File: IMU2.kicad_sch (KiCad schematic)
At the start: 3 parts, among them U3 262-BMI088

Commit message: multiple chainges on PCB
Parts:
- added BMI3, BMI3_SCL1, BMI3_SDA1: 0, Resistor_SMD:R_0603_1608Metric, symbol #dzdb:g_res/R-0-0603
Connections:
- net BMI_IN_3.3V: now also BMI3.1; no longer U3.14 (CSB1), U3.7 (PS)
- net IMU_SCL: now also BMI3_SCL1.1; no longer U3.8 (SCL/SCK)
- net IMU_SDA: now also BMI3_SDA1.1; no longer U3.9 (SDA/SDI)
- new net: BMI3_SCL1.2, U3.8 (SCL/SCK)
- new net: BMI3.2, U3.14 (CSB1), U3.7 (PS)
- new net: BMI3_SDA1.2, U3.9 (SDA/SDI)

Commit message: nearly complete with the PCB
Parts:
- renumbered BMI3 to BMI2, BMI3_SCL1 to BMI2_SCL1, BMI3_SDA1 to BMI2_SDA1, U3 to U2
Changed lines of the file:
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@@
 		(on_board yes)
 		(dnp no)
-		(property "Reference" "BMI3_SCL1"
+		(property "Reference" "BMI2_SCL1"
 			(at 119.38 99.06 90)
 			(effects
@@
 			(project "nautilus_mainboard"
 				(path "/ce1819b2-f280-40ed-834f-6fe4d12f809d/bdf8f7d6-a5ee-4741-925d-5019e8cbdfce/a7ffb13a-d9ae-4b81-b70f-0aefcfc6ef00"
-					(reference "BMI3_SCL1")
+					(reference "BMI2_SCL1")
 					(unit 1)
 				)
@@
 		(on_board yes)
 		(dnp no)
-		(property "Reference" "BMI3"
+		(property "Reference" "BMI2"
 			(at 119.38 88.9 90)
 			(effects
@@
 			(project "nautilus_mainboard"
 				(path "/ce1819b2-f280-40ed-834f-6fe4d12f809d/bdf8f7d6-a5ee-4741-925d-5019e8cbdfce/a7ffb13a-d9ae-4b81-b70f-0aefcfc6ef00"
-					(reference "BMI3")
+					(reference "BMI2")
 					(unit 1)
 				)
@@
 		(on_board yes)
 		(dnp no)
-		(property "Reference" "BMI3_SDA1"
+		(property "Reference" "BMI2_SDA1"
 			(at 119.38 101.6 90)
 			(effects
@@
 			(project "nautilus_mainboard"
 				(path "/ce1819b2-f280-40ed-834f-6fe4d12f809d/bdf8f7d6-a5ee-4741-925d-5019e8cbdfce/a7ffb13a-d9ae-4b81-b70f-0aefcfc6ef00"
-					(reference "BMI3_SDA1")
+					(reference "BMI2_SDA1")
 					(unit 1)
 				)
@@
 		(dnp no)
 		(fields_autoplaced yes)
-		(property "Reference" "U3"
+		(property "Reference" "U2"
 			(at 144.78 73.66 0)
 			(effects
@@
 			(project "nautilus_mainboard"
 				(path "/ce1819b2-f280-40ed-834f-6fe4d12f809d/bdf8f7d6-a5ee-4741-925d-5019e8cbdfce/a7ffb13a-d9ae-4b81-b70f-0aefcfc6ef00"
-					(reference "U3")
+					(reference "U2")
 					(unit 1)
 				)

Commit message: chore: Many routing changes
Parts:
- removed BMI2, BMI2_SCL1, BMI2_SDA1: 0, Resistor_SMD:R_0603_1608Metric, symbol #dzdb:g_res/R-0-0603
- added R48, R49, R52: 0, Resistor_SMD:R_0603_1608Metric, symbol #dzdb:g_res/R-0-0603
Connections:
- net IMU_SCL: now also R48.1
- net IMU_SDA: now also R49.1
- net at U2.8 (SCL/SCK): now also R48.2
- net at U2.14 (CSB1), U2.7 (PS): now also R52.2
- net at U2.9 (SDA/SDI): now also R49.2
- net BMI_IN_3.3V renamed BMI_In_3.3V
- net BMI_In_3.3V: now also R52.1

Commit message: chore: more cleanup
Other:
- company: (none) -> Davide
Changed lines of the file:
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@@
 	(generator_version "9.0")
 	(paper "A4")
+	(title_block
+		(date "2025-11-18")
+		(company "Davide")
+	)
 	(text "Acc: 0x19\nGyro: 0x69"
 		(exclude_from_sim no)

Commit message: chore: Loads of redoing stuff. Added a Changelog
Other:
- title: (none) -> Nautilus_Mainboard
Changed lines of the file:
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@@
 	(paper "A4")
 	(title_block
+		(title "Nautilus_Mainboard")
 		(date "2025-11-19")
 		(rev "0")

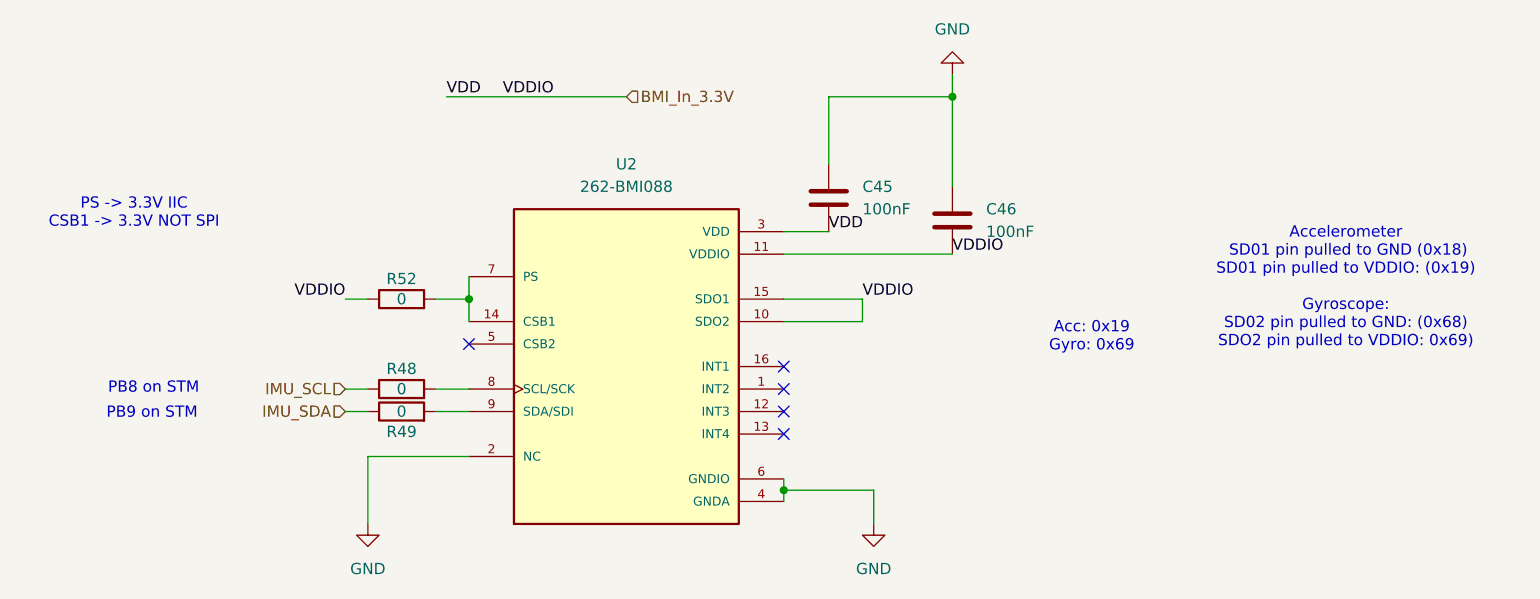
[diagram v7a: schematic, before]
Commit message: chore: routed the Jumpers (incomplete) fix: removed all leftover 0Ohm resistors
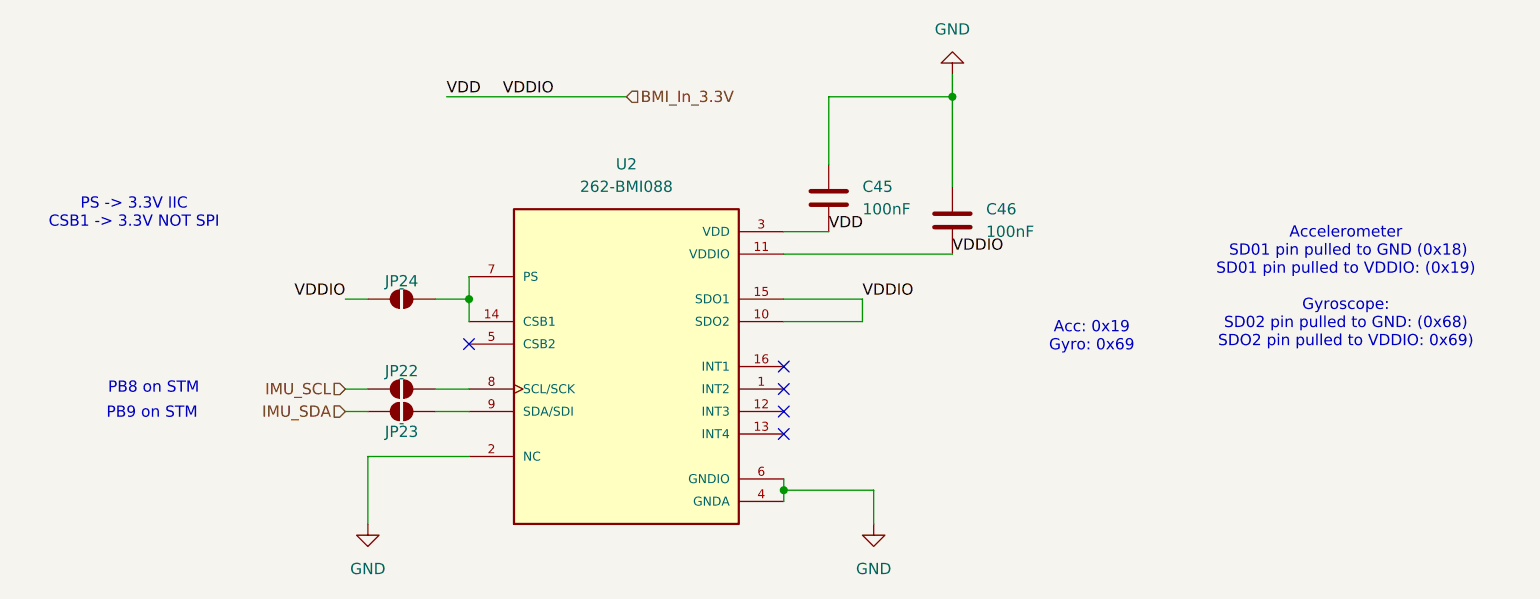
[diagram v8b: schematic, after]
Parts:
- removed R48, R49, R52: 0, Resistor_SMD:R_0603_1608Metric, symbol #dzdb:g_res/R-0-0603
- added JP22, JP23, JP24: -, Jumper:SolderJumper-2_P1.3mm_Open_RoundedPad1.0x1.5mm, symbol #dzdb:g_mech/Jumper-2P1.3mm_Rounded
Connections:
- net BMI_In_3.3V: now also JP24.1 (A)
- net IMU_SCL: now also JP22.1 (A)
- net IMU_SDA: now also JP23.1 (A)
- net at U2.14 (CSB1), U2.7 (PS): now also JP24.2 (B)
- net at U2.8 (SCL/SCK): now also JP22.2 (B)
- net at U2.9 (SDA/SDI): now also JP23.2 (B)
